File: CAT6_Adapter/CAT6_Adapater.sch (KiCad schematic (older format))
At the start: 7 parts, among them J1 RJ45, J2 RJ45, P1 CONN_02X04, P2 CONN_01X02, U1 MCP2551-I/P

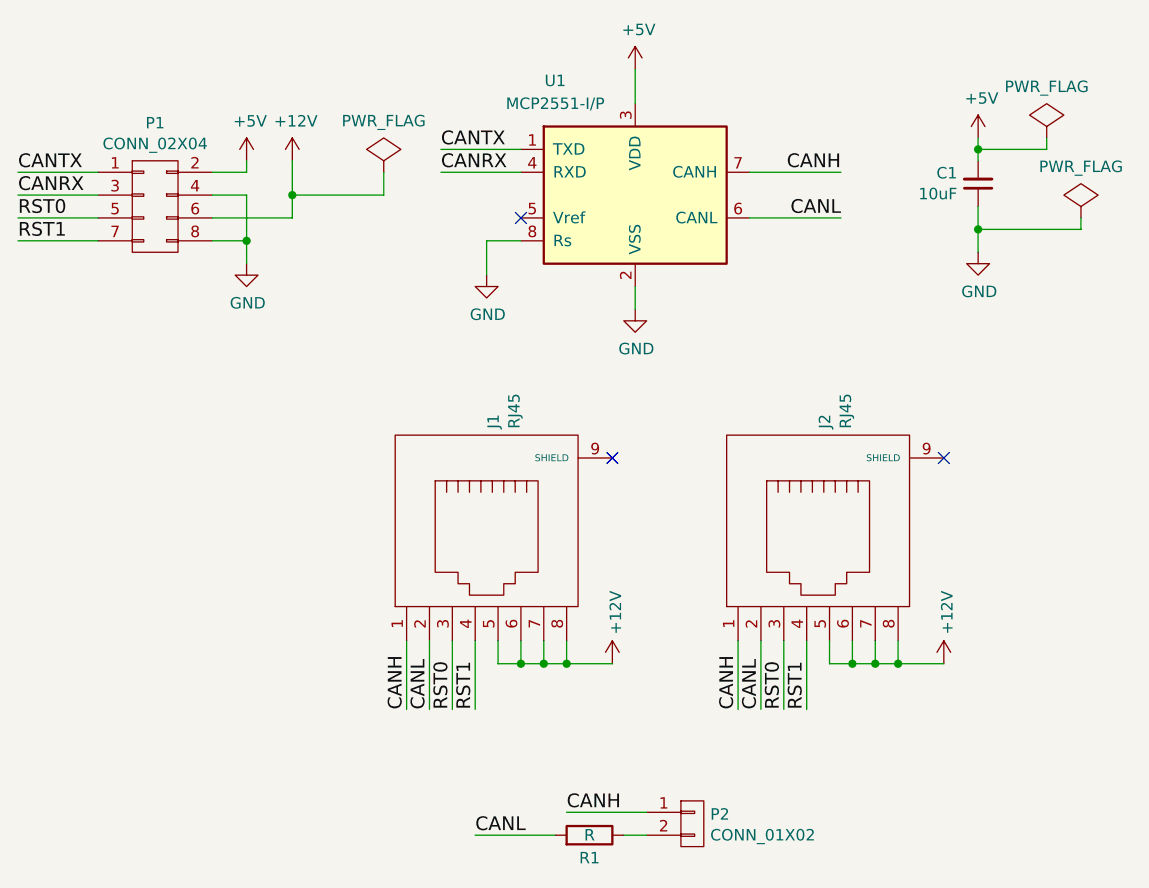
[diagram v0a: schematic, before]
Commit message: CPL and CAT6 Adapter
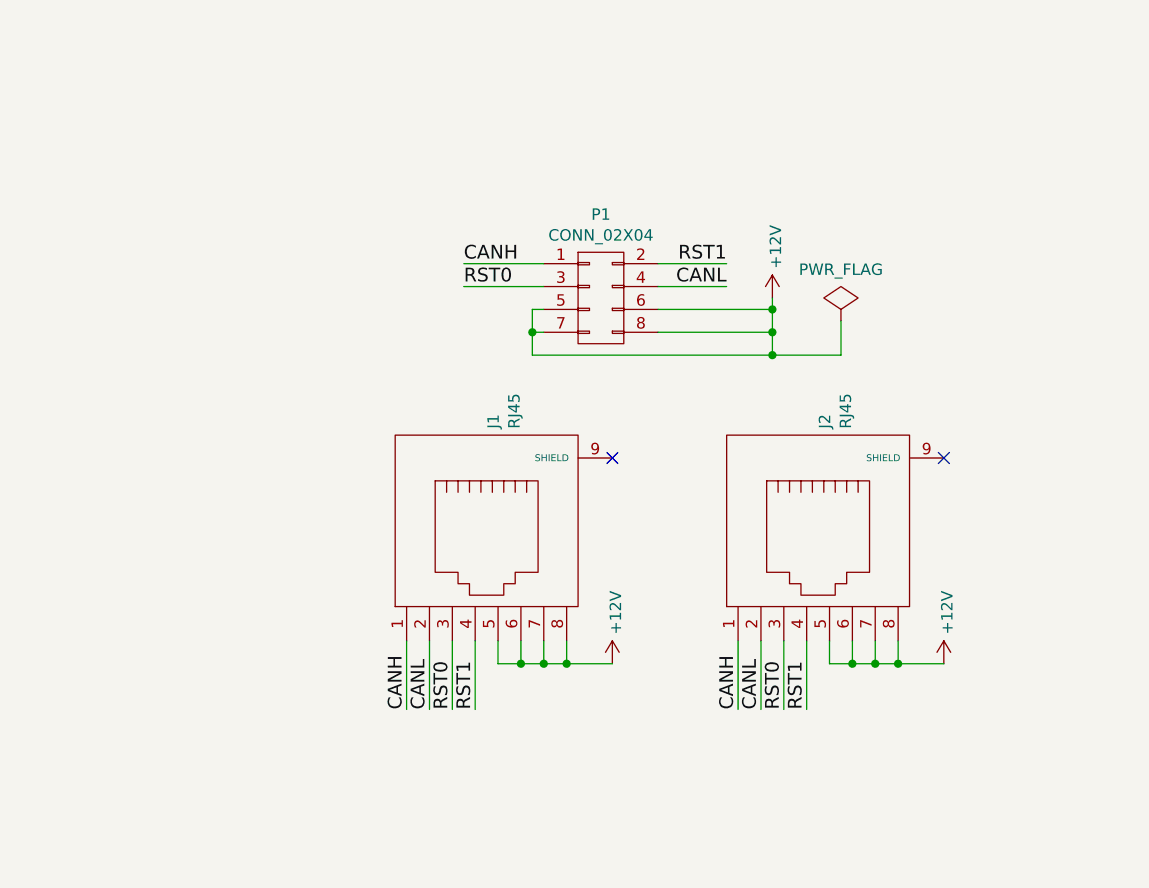
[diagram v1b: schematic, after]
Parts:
- removed C1: 10uF, Capacitors_SMD:C_0805, symbol C_Small
- removed P2: CONN_01X02, Pin_Headers:Pin_Header_Straight_1x02, symbol CONN_01X02
- removed R1: R, Resistors_SMD:R_0805, symbol R
- removed U1: MCP2551-I/P, UNCAMotorsports:SOIC-8, symbol MCP2551-I/P
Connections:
- net +5V is gone; now on net RST1: P1.2 (P2)
- net CANRX is gone; now on net RST0: P1.3 (P3)
- net CANTX is gone; now on net CANH: P1.1 (P1)
- net +12V: now also P1.5 (P5), P1.7 (P7), P1.8 (P8)
- net CANL: now also P1.4 (P4)
- net RST0: no longer P1.5 (P5)
- net RST1: no longer P1.7 (P7)
- removed net GND: P1.4 (P4), P1.8 (P8)
- no-connect marks 3 -> 2
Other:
- moved on the sheet: P1
